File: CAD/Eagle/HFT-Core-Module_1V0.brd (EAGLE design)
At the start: 96.5 x 96.5 mm, 352 parts, among them Q0521 ABS07-32.768KHZ, Q0911 ABM3B-16MHZ-10-R50-1-U, T0801 MMBT2222, T0802 MMBT2222, T0803 MMBT2222, U0111 STM32L4Z_144PIN_SMPS, U0431 PAM2305AAB120, U0601 LM4120IM5-3.0, U0611 MAX5217, U0631 CFPT-141-20MHZ, U0641 OPA354, U0701 Si5338, U0801 NHD-C0220BIZ_2X20CHARS, U0901 AX5243, U1001 AX5243, U1101 MCP3911A0-E-SS, U1111 MAX5136AGTG+, U1121 OPA354, U1131 OPA354, U1141 OPA354, U1601 SOLARPANEL_3V3_5MA1_25MM_X_20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, U1602 SPV1040T, U1701 TS5A23166, U1801 PAM2305AAB330, U1901 TS5A23166, U2001 TS5A23166, U2101 TS5A23166, U2301 MPU-9250, U401 MS5607-02BA03, U501 SHT31-DIS, X0861 TTE_EN11-HSM, X1401 SMA_SMT_AMPHENOL-901-143, X1411 SMA_SMT_AMPHENOL-901-143, X1501 CUI SJ1-3535NS, X1511 CUI SJ1-3535NS, X511 2X20/90_1MM27_HARWIN_M50-3202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, X512 2X20/90_1MM27_HARWIN_M50-3202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, X521 2X20/90_1MM27_HARWIN_M50-3202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, X522 2X20/90_1MM27_HARWIN_M50-3202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, X531 2X20/90_1MM27_HARWIN_M50-3202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, X532 2X20/90_1MM27_HARWIN_M50-3202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

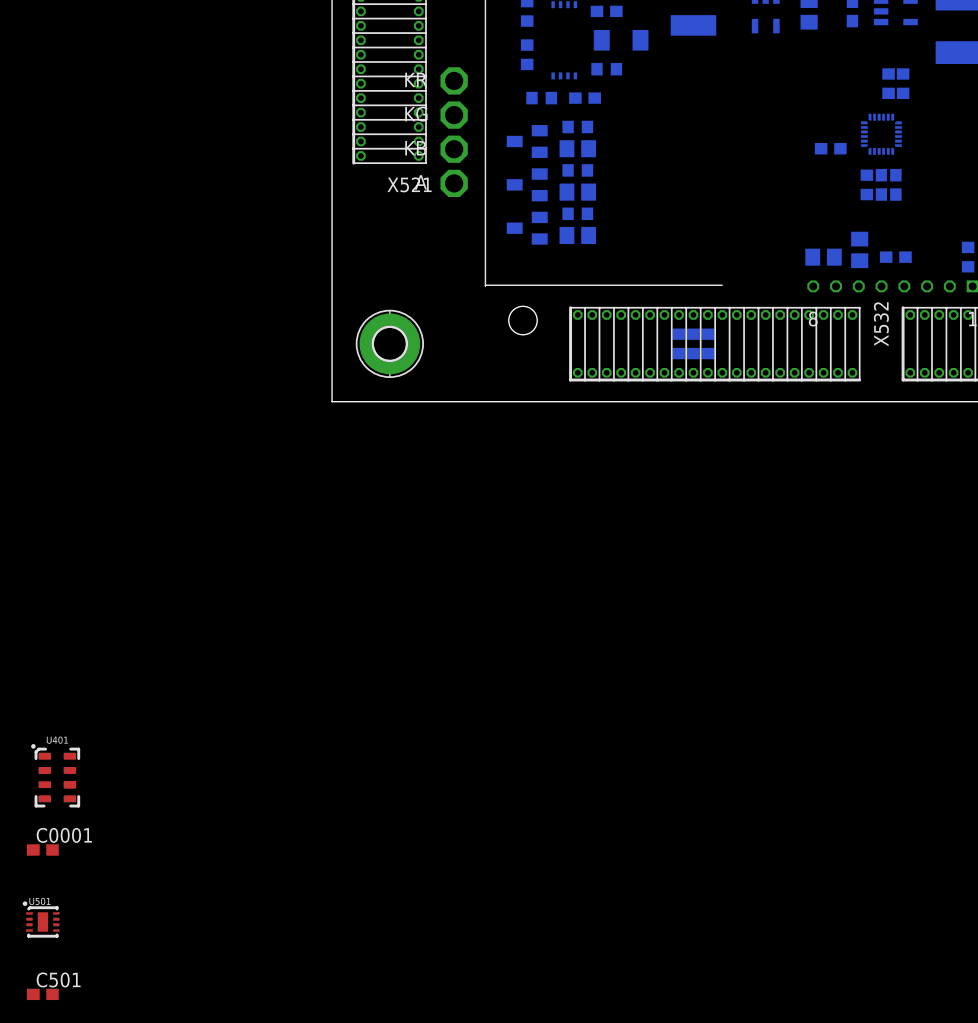
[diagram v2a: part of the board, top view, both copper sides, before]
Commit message: HW_1V0 - SX1276 added to the board - before removing one AX5243
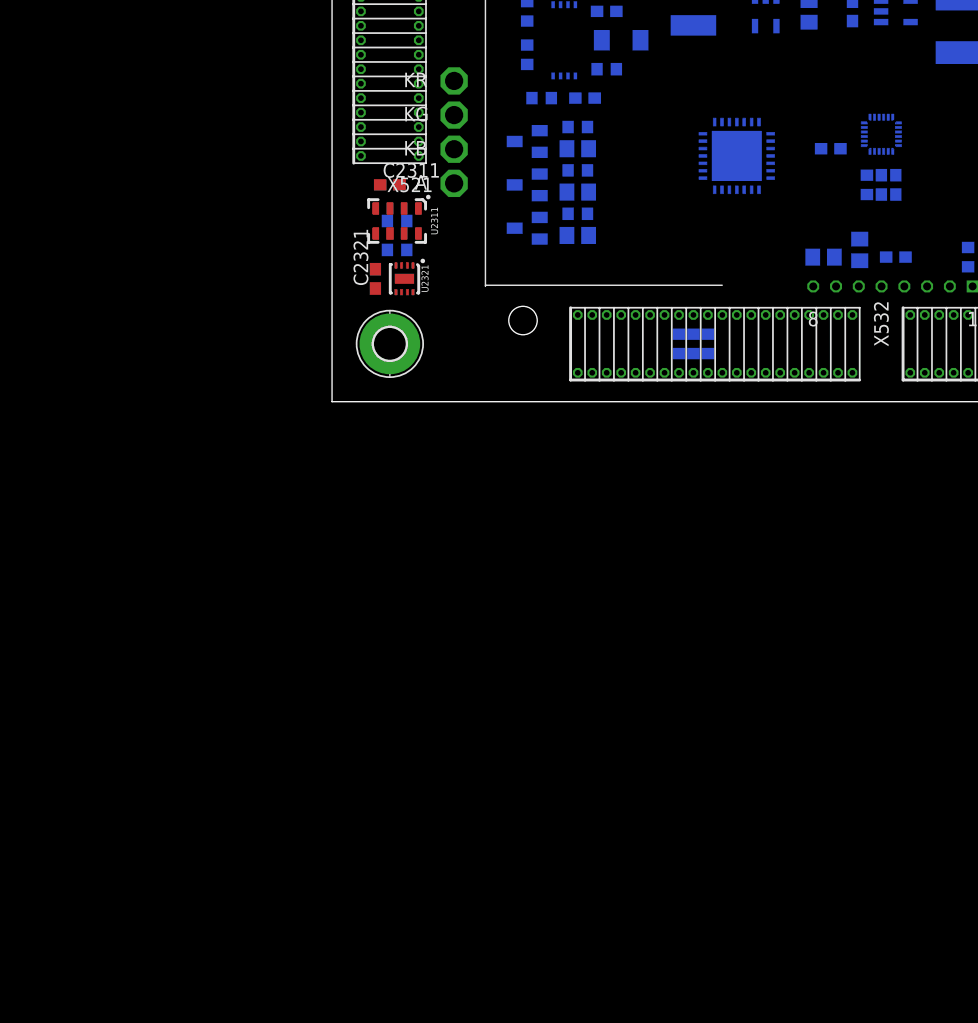
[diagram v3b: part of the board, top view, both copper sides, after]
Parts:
- removed C0001, C501: 100nF, rcl:C0603
- removed R2311, R2312: 3.9kR, rcl:R0603
- removed U401: MS5607-02BA03, df4iah_sensors:MS5607-02BA
- removed U501: SHT31-DIS, df4iah_sensors:DFN8/SHT
- added C2311, C2321: 100nF, rcl:C0603
- added R2331, R2332: 3.9kR, rcl:R0603
- added U2311: MS5607-02BA03, df4iah_sensors:MS5607-02BA
- added U2321: SHT31-DIS, df4iah_sensors:DFN8/SHT
- added U2401: SX1276, df4iah_rf:QFN28-6X6-0P65-PAD
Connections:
- net +3V3: now also C2311.1, C2321.1, R2331.2, R2332.2, U2311.1, U2311.2, U2311.4, U2321.5, U2321.6; no longer C0001.1, C501.1, R2311.2, R2312.2, U401.1, U401.2, U401.4, U501.5, U501.6
- net GND: now also C2311.2, C2321.2, U2311.3, U2321.2, U2321.7, U2321.8, U2321.9, U2401.15, U2401.23, U2401.26, U2401.29; no longer C0001.2, C501.2, U401.3, U501.2, U501.7, U501.8, U501.9
- net MCU_I2C4_SCL: now also R2332.1, U2311.8, U2321.4; no longer R2312.1, U401.8, U501.4
- net MCU_I2C4_SDA: now also R2331.1, U2311.7, U2321.1; no longer R2311.1, U401.7, U501.1

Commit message: HW_1V0_trySX - work-of-the-day for SX1276
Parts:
- removed C1001, C1002, C1003: 100nF, rcl:C0603
- removed C1011: 10pF, rcl:C0603
- removed C1012: 6.8pF, rcl:C0603
- removed C_AX2_A2, C_AX2_A3, C_AX2_B2, C_AX2_F2, C_AX2_M1: 4.7pF, rcl:C0603
- removed C_AX2_C1, C_AX2_C2, C_AX2_M2: 0pF, rcl:C0603
- removed C_AX2_T1, C_AX2_T2: 4.3pF, rcl:C0603
- removed L_AX2_1, L_AX2_B1, L_AX2_B2, L_AX2_F1: 22nH, rcl:R0603
- removed L_AX2_C1, L_AX2_C2: 100nH, rcl:R0603
- removed L_AX2_T1, L_AX2_T2: 43nH, rcl:R0603
- removed R1031, R1032: 100kR, rcl:R0603
- removed R1041, R1051, R1061: 47R, rcl:R0603
- removed TP_AX2_ADC1, TP_AX2_ADC2, TP_AX2_IRQ, TP_AX2_TCXO_EN: PTR1TP06R, testpad:TP06R
- removed U1001: AX5243, df4iah_rf:QFN20-4X4-0P5-PAD
- added C2401: 1u, rcl:C0603
- added C2402, C2403, C2404, C2405, C2406, C2407: 100n, rcl:C0603
- added C2411, C2412: 4.7p, rcl:C0603
- added Q2411: ABM03B-32.000MHZ, df4iah_crystal:ABM03B
- added R2411: 0R, rcl:R0603
- added R2421: 100R, rcl:R0603
- added R2431: 47R, rcl:R0603
- moved U2401 29.3 mm to (64.8, 19.1)
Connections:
- removed net AX2_ADC1: R1031.1, TP_AX2_ADC1.TP, U1001.17
- removed net AX2_ADC2: R1032.1, TP_AX2_ADC2.TP, U1001.18
- removed net AX2_ANTN: C_AX2_C2.1, C_AX2_T2.1, L_AX2_C2.1, U1001.4
- removed net AX2_ANTP: C_AX2_C1.1, C_AX2_T1.1, L_AX2_C1.1, U1001.3
- removed net AX2_B1: C_AX2_M1.1, L_AX2_B1.1, L_AX2_T1.2
- removed net AX2_B2: C_AX2_B2.1, C_AX2_M2.1, L_AX2_B2.2, L_AX2_T2.2
- removed net AX2_CLK16P: C1011.2, C1012.1, U1001.20
- removed net AX2_COMB1: C_AX2_A2.1, C_AX2_B2.2, C_AX2_F2.1, L_AX2_B1.2, L_AX2_F1.1
- removed net AX2_L1: L_AX2_1.1, U1001.8
- removed net AX2_L2: L_AX2_1.2, U1001.7
- removed net AX2_T1: C_AX2_T1.2, L_AX2_T1.1
- removed net AX2_T2: C_AX2_T2.2, L_AX2_T2.1
- removed net AX2_VDD1: C1002.2, U1001.1
- removed net AX2_VDD5: C1003.2, U1001.5
- removed net MCU_AX2_GPO1: R1061.2, TP_AX2_TCXO_EN.TP, U1001.15
- removed net MCU_AX2_IRQ: R1051.2, TP_AX2_IRQ.TP, U1001.14
- removed net MCU_AX2_MISO: R1041.2, U1001.12
- removed net MCU_SPI3_AX2_SEL: R0254.2, U1001.10
- new net MCU_SPI3_SX_SEL: R0254.2, U2401.19
- new net SX_!RESET: R2421.1
- new net SX_!RESET_R: R2421.2, U2401.7
- new net SX_MISO: R2431.2, U2401.17
- new net SX_VR_ANA: C2406.2, U2401.2
- new net SX_VR_DIG: C2407.2, U2401.4
- new net SX_VR_PA: C2405.2, U2401.25
- new net SX_XTA: C2411.1, Q2411.1, U2401.5
- new net SX_XTB: R2411.1, U2401.6
- new net XTB_R: C2412.2, Q2411.3, R2411.2
- net +3V3: now also C2401.1, C2402.2, C2403.2, C2404.2, U2401.14, U2401.24, U2401.3; no longer C1001.1, U1001.16
- net AX1_SYSCLK_R: no longer C1011.1
- net AX2_ANT: no longer C_AX2_A3.1, C_AX2_F2.2, L_AX2_F1.2
- net GND: now also C2401.2, C2402.1, C2403.1, C2404.1, C2405.1, C2406.1, C2407.1, C2411.2, C2412.1, Q2411.2, Q2411.4; no longer C1001.2, C1002.1, C1003.1, C1012.2, C_AX2_A2.2, C_AX2_A3.2, C_AX2_C1.2, C_AX2_C2.2, C_AX2_M1.2, C_AX2_M2.2, L_AX2_B2.1, L_AX2_C1.2, L_AX2_C2.2, R1031.2, R1032.2, U1001.2, U1001.21
- net MCU_SPI3_MOSI: now also U2401.18; no longer U1001.13
- net MCU_SPI3_SCK: now also U2401.16; no longer U1001.11
- net PC11: now also R2431.1; no longer R1041.1
- net PF13: no longer R1061.1
- net PG0: no longer R1051.1

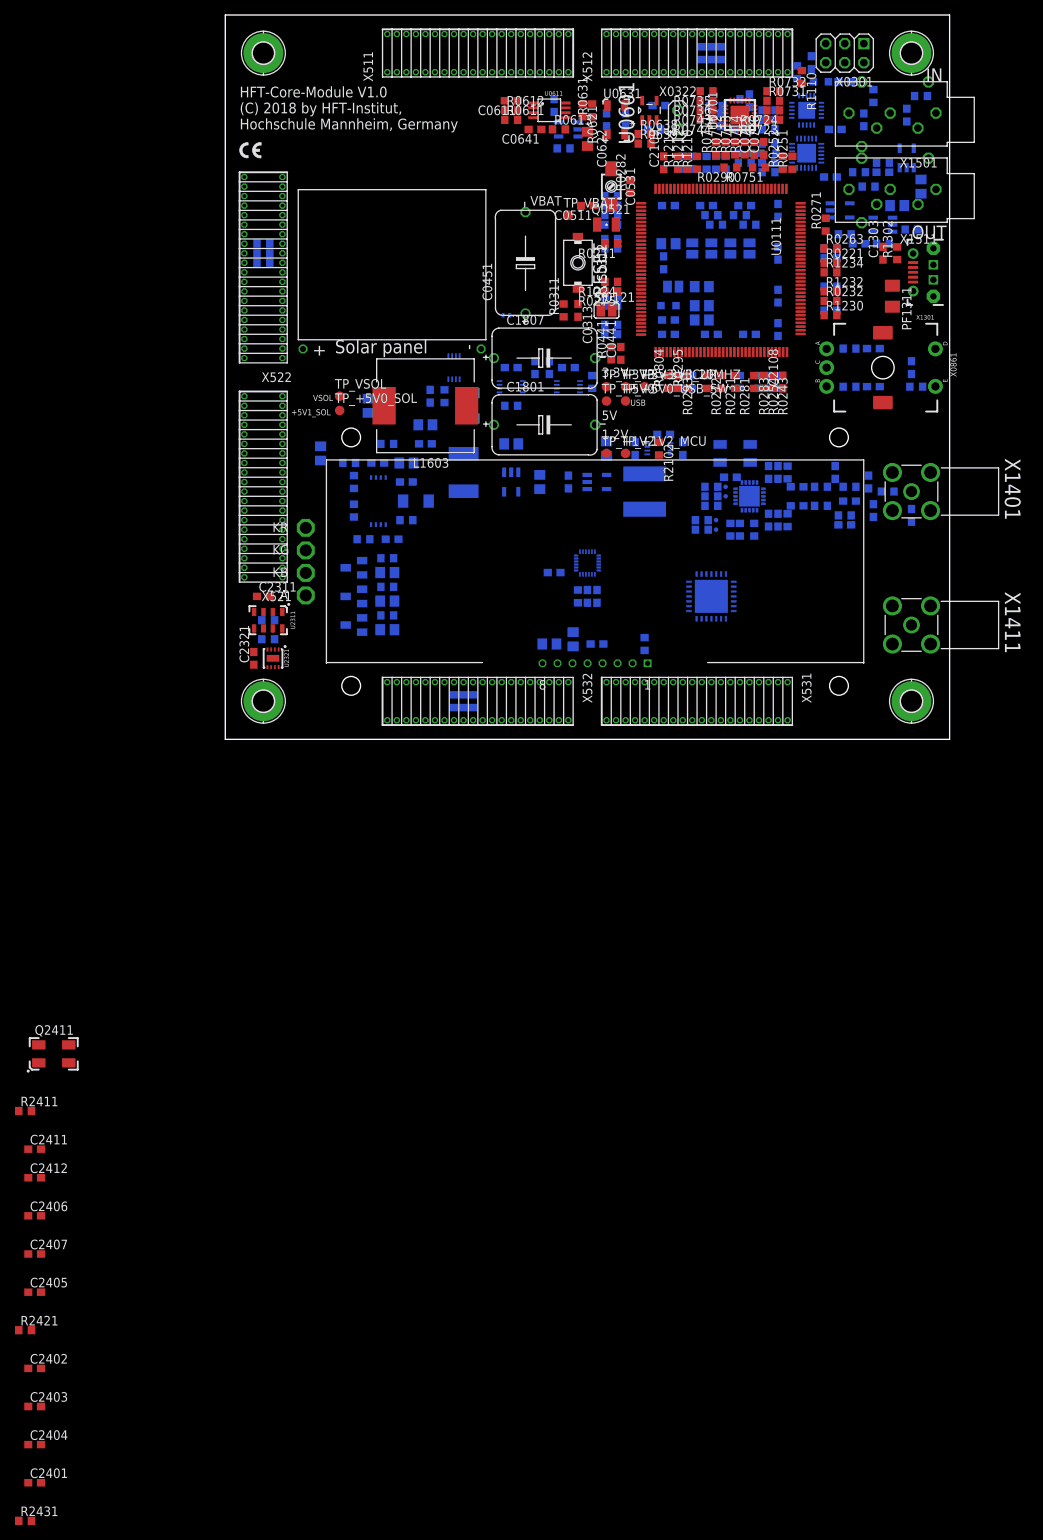
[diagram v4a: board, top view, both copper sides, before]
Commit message: HW_1V0_trySX - reordering and renumbering all parts
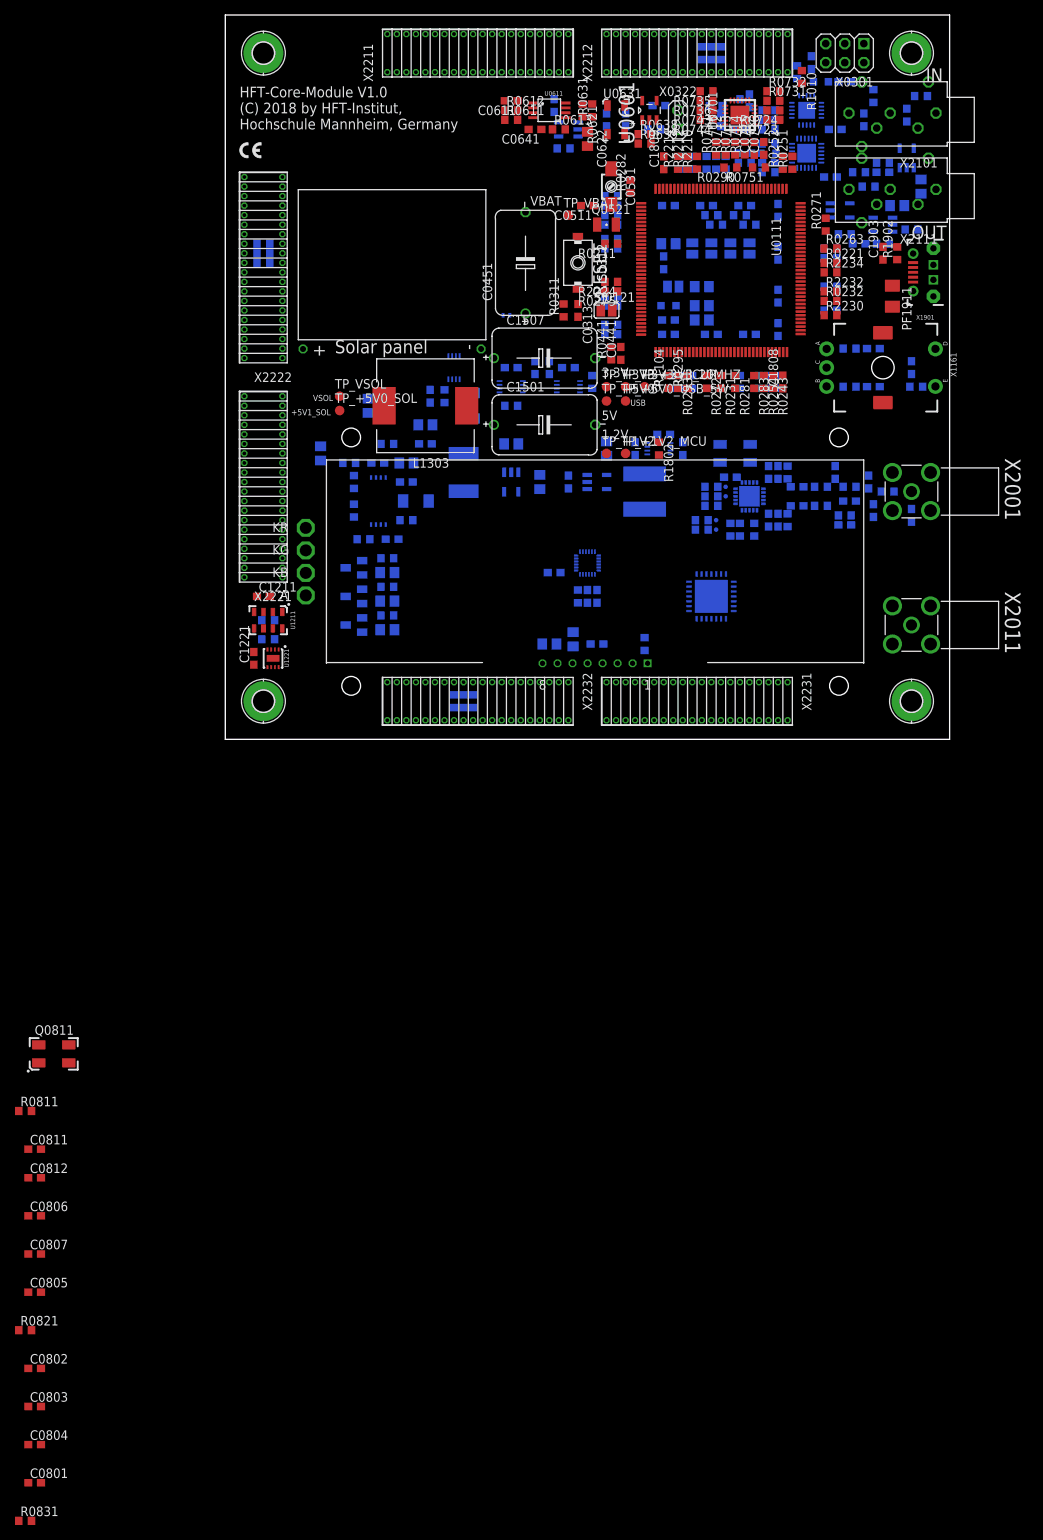
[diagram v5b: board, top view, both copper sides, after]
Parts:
- removed C0831, C1901, C2001, C2003, C2101, C2102: 100nF, rcl:C0603
- removed C2411: 4.7p, rcl:C0603
- removed R0804, R0807: 2.2kR, rcl:R0603
- removed R0805, R0808: 1.8kR, rcl:R0603
- removed R0806, R0809: 10R, rcl:R0805
- removed R0841: 33kR, rcl:R0603
- removed R1302: 330kR, rcl:R0603
- removed R2331, R2332: 3.9kR, rcl:R0603
- removed U1901, U2001, U2101: TS5A23166, df4iah_sc-switches:R-PDSO-G8
- removed U2401: SX1276, df4iah_rf:QFN28-6X6-0P65-PAD
- added C1011, C1401, C1703: 100nF, rcl:C0603
- added C1031: 220nF, df4iah_rcl:C0603
- added C1301: 10uF, rcl:C0805
- added C1501: 1F_EEC-S5R5H105N, df4iah_rcl:W14MM_D8MM_P13MM5
- added C1502: 47uF, rcl:C0805
- added R1004, R1005: 22kR, rcl:R0603
- added R1006, R1007, R1008, R1009, R2231, R2232: 47R, rcl:R0603
- added R1041: 10kR, rcl:R0603
- added R1402: 33kR, rcl:R0603
- added U1001: MCP3911A0-E-SS, df4iah_adc:QFN20_P0MM5_CTRPAD
- added U1301: SOLARPANEL_3V3_5MA1_25MM_X_20MM, df4iah_supply:SOLARPANEL_3V3_5MA1_25MM_X_20MM
- added U1401: TS5A23166, df4iah_sc-switches:R-PDSO-G8
- added U1501: PAM2305AAB330, df4iah_powersupply:SOT95P280X145-5N
- C0811: value 1uF -> 4.7p; device rcl:C0805 -> rcl:C0603
- C1111: value 100nF -> 1uF; device rcl:C0603 -> rcl:C0805
- C1131: value 220nF -> 100nF; device df4iah_rcl:C0603 -> rcl:C0603
- C1303: value 1nF -> 100nF; device df4iah_rcl:C0603 -> rcl:C0603
- C1601: value 10uF -> 100nF; device rcl:C0805 -> rcl:C0603
- C1801: value 1F_EEC-S5R5H105N -> 100nF; device df4iah_rcl:W14MM_D8MM_P13MM5 -> rcl:C0603
- C1802: value 47uF -> 100nF; device rcl:C0805 -> rcl:C0603
- C1903: value 100nF -> 1nF; device rcl:C0603 -> df4iah_rcl:C0603
- R1104: value 22kR -> 2.2kR
- R1105: value 22kR -> 1.8kR
- R1106, R1109: value 47R -> 10R; device rcl:R0603 -> rcl:R0805
- R1107: value 47R -> 2.2kR
- R1108: value 47R -> 1.8kR
- R1141: value 10kR -> 33kR
- R1231, R1232: value 47R -> 3.9kR
- R1902: value 33kR -> 330kR
- U0801: value NHD-C0220BIZ_2X20CHARS -> SX1276; device df4iah_lcd:NHD-C0220BIZ_2X20CHARS -> df4iah_rf:QFN28-6X6-0P65-PAD
- U1101: value MCP3911A0-E-SS -> NHD-C0220BIZ_2X20CHARS; device df4iah_adc:QFN20_P0MM5_CTRPAD -> df4iah_lcd:NHD-C0220BIZ_2X20CHARS
- U1601: value SOLARPANEL_3V3_5MA1_25MM_X_20MM -> TS5A23166; device df4iah_supply:SOLARPANEL_3V3_5MA1_25MM_X_20MM -> df4iah_sc-switches:R-PDSO-G8
- U1801: value PAM2305AAB330 -> TS5A23166; device df4iah_powersupply:SOT95P280X145-5N -> df4iah_sc-switches:R-PDSO-G8
- moved C0811 96.1 mm to (-25.4, -54.6), flipped to the top, turned to 0 degrees
- moved R1105 92.0 mm to (21.6, 20.3), turned to 0 degrees
- moved R1232 88.1 mm to (5.71, 13.3), flipped to the bottom
- moved R1231 85.5 mm to (5.71, 15.9), turned to 0 degrees
- moved R1109 83.8 mm to (21.6, 14.6)
- moved R1108 83.3 mm to (21.6, 16.5)
- moved R1106 82.8 mm to (21.6, 18.4)
- moved C1131 73.5 mm to (49.5, 12.7)
- moved C1303 70.4 mm to (24.1, 34.3), flipped to the bottom, turned to 180 degrees
- moved C1111 70.4 mm to (43.2, 12.7), turned to 180 degrees
- moved U1101 66.0 mm to (49.3, 24.1), flipped to the top
- moved R1141 60.8 mm to (55.9, 12.7), turned to 270 degrees
- moved R1104 50.8 mm to (59.1, 47.6), flipped to the top, turned to 90 degrees
- moved C1903 47.0 mm to (87.6, 64.8), flipped to the top
- moved R1902 44.1 mm to (89.5, 64.8), flipped to the top, turned to 90 degrees
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- renumbered C0821 to C1121, C0861 to C1161, C0862 to C1162, C0871 to C1171, C1101 to C1001, C1102 to C1002, C1103 to C1003, C1104 to C1004, C1105 to C1005, C1112 to C1012, C1113 to C1013, C1132 to C1032, C1141 to C1041, C1142 to C1042, C1602 to C1302, C1604 to C1304, C1605 to C1305, C1606 to C1306, C1805 to C1505, C1806 to C1506, C1807 to C1507, C2103 to C1803, C2108 to C1808, C2109 to C1809, C2301 to C1201, C2302 to C1202, C2303 to C1203, C2311 to C1211, C2321 to C1221, C2401 to C0801, C2402 to C0802, C2403 to C0803, C2404 to C0804, C2405 to C0805, C2406 to C0806, C2407 to C0807, C2412 to C0812, D1603 to D1303, D1701 to D1401, H2201 to H2301, H2202 to H2302, H2203 to H2303, H2204 to H2304, L1102 to L1002, L1112 to L1012, L1603 to L1303, L1804 to L1504, PF1311 to PF1911, Q2411 to Q0811, R0801 to R1101, R0802 to R1102, R0803 to R1103, R0861 to R1161, R0862 to R1162, R0871 to R1171, R1110 to R1010, R1114 to R1014, R1131 to R1031, R1132 to R1032, R1135 to R1035, R1142 to R1042, R1145 to R1045, R1210 to R2210, R1211 to R2211, R1212 to R2212, R1213 to R2213, R1214 to R2214, R1215 to R2215, R1216 to R2216, R1217 to R2217, R1220 to R2220, R1221 to R2221, R1222 to R2222, R1223 to R2223, R1224 to R2224, R1225 to R2225, R1226 to R2226, R1227 to R2227, R1230 to R2230, R1233 to R2233, R1234 to R2234, R1235 to R2235, R1236 to R2236, R1237 to R2237, R1604 to R1304, R1605 to R1305, R1606 to R1306, R1607 to R1307, R1608 to R1308, R1609 to R1309, R2002 to R1602, R2102 to R1802, R2301 to R1201, R2411 to R0811, R2421 to R0821, R2431 to R0831, T0801 to T1101, T0802 to T1102, T0803 to T1103, U1111 to U1011, U1121 to U1021, U1131 to U1031, U1141 to U1041, U1602 to U1302, U2301 to U1201, U2311 to U1211, U2321 to U1221, X0861 to X1161, X1301 to X1901, X1401 to X2001, X1411 to X2011, X1501 to X2101, X1511 to X2111, X511 to X2211, X512 to X2212, X521 to X2221, X522 to X2222, X531 to X2231, X532 to X2232
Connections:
- net +1V2: now also C1801.1, U1801.1, U1801.5; no longer C2101.1, U2101.1, U2101.5
- net +3V3: now also C1131.1, C1601.1, C1701.1, C1802.1, R1231.2, R1232.2, U0801.14, U0801.24, U0801.3, U1101.12, U1101.5, U1501.4, U1601.1, U1601.5, U1601.8, U1701.1, U1701.5, U1701.8, U1801.8; no longer C0831.1, C1901.1, C2001.1, C2102.1, R2331.2, R2332.2, U0801.12, U0801.5, U1801.4, U1901.1, U1901.5, U1901.8, U2001.1, U2001.5, U2001.8, U2101.8, U2401.14, U2401.24, U2401.3
- net +3V3_20MHZ: now also C1703.1, U1701.2, U1701.6; no longer C1903.1, U1901.2, U1901.6
- net +3V3_HICUR: now also C1011.1, C1603.1, U1001.19, U1601.2, U1601.6; no longer C1111.1, C2003.1, U1101.19, U2001.2, U2001.6
- net +5V0: now also C1501.+, C1502.1, U1501.1, U1501.3; no longer C1801.+, C1802.1, U1801.1, U1801.3
- net GND: now also C0811.2, C1011.2, C1131.2, C1301.2, C1303.2, C1401.2, C1501.-, C1502.2, C1703.2, C1801.2, C1903.1, R1004.1, R1005.1, R1106.1, R1108.1, R1109.1, R1141.1, R1402.1, U0801.15, U0801.23, U0801.26, U0801.29, U1001.2, U1001.21, U1001.4, U1001.5, U1001.7, U1001.8, U1301.-VSOL, U1401.4, U1501.2, U1601.4, U1801.4; no longer C0831.2, C1111.2, C1303.1, C1801.-, C1901.2, C1903.2, C2001.2, C2003.2, C2101.2, C2102.2, C2411.2, R0805.1, R0806.1, R0808.1, R0809.1, R0841.1, R1104.1, R1302.1, U0801.4, U1101.2, U1101.21, U1101.5, U1101.7, U1101.8, U1601.-VSOL, U1801.2, U1901.4, U2001.4, U2101.4, U2401.15, U2401.23, U2401.26, U2401.29
- net LCD_C1+: now also C1111.2, U1101.7; no longer C0811.2, U0801.7
- net LCD_C1-: now also C1111.1, U1101.8; no longer C0811.1, U0801.8
- net LCD_VOUT: now also U1101.6; no longer U0801.6
- net LED_B_B: now also R1107.1, R1108.2; no longer R0807.1, R0808.2
- net LED_B_E: now also R1109.2; no longer R0809.2
- net LED_B_K: now also U1101.11; no longer U0801.11
- net LED_G_B: now also R1104.1, R1105.2; no longer R0804.1, R0805.2
- net LED_G_E: now also R1106.2; no longer R0806.2
- net LED_G_K: now also U1101.10; no longer U0801.10
- net LED_R_K: now also U1101.9; no longer U0801.9
- net MAX5136_OUT0_R: now also C1031.1; no longer C1131.1
- net MAX5136_OUT0_SUM: now also C1031.2; no longer C1131.2
- net MAX5136_OUT1: now also R1041.1; no longer R1141.1
- net MAX5136_OUT1_R: now also R1041.2; no longer R1141.2
- net MCP3911_!DR: now also R1006.1, U1001.11; no longer R1106.1, U1101.11
- net MCP3911_CH0+: now also R1004.2, U1001.1; no longer R1104.2, U1101.1
- net MCP3911_CH1+: now also R1005.2, U1001.3; no longer R1105.2, U1101.3
- net MCP3911_MDAT0: now also R1008.1, U1001.10; no longer R1108.1, U1101.10
- net MCP3911_MDAT1: now also R1009.1, U1001.9; no longer R1109.1, U1101.9
- net MCP3911_REFINOUT: now also U1001.6; no longer U1101.6
- net MCP3911_SDO: now also R1007.1, U1001.16; no longer R1107.1, U1101.16
- net MCU_20MHZ_EN: now also R1702.2, U1701.3, U1701.7; no longer R1902.2, U1901.3, U1901.7
- net MCU_HICUR_EN: now also U1601.3, U1601.7; no longer U2001.3, U2001.7
- net MCU_I2C4_SCL: now also R1232.1, U1101.2; no longer R2332.1, U0801.2
- net MCU_I2C4_SDA: now also R1231.1, U1101.3; no longer R2331.1, U0801.3
- net MCU_LCD_!RST: now also R1141.2, U1101.1; no longer R0841.2, U0801.1
- net MCU_SPI3_AUDIO_ADC_!RESET: now also U1001.18; no longer U1101.18
- net MCU_SPI3_AUDIO_ADC_SEL: now also U1001.14; no longer U1101.14
- net MCU_SPI3_MOSI: now also U0801.18, U1001.17; no longer U1101.17, U2401.18
- net MCU_SPI3_SCK: now also U0801.16, U1001.15; no longer U1101.15, U2401.16
- net MCU_SPI3_SX_SEL: now also U0801.19; no longer U2401.19
- net MCU_VDD12: now also U1801.2, U1801.6; no longer U2101.2, U2101.6
- net MCU_VDD12_EN: now also U1801.3, U1801.7; no longer U2101.3, U2101.7
- net MCU_VUSB_EN: now also R1402.2, U1401.3, U1401.7; no longer R1702.2, U1701.3, U1701.7
- net MVP3911_AVDD: now also U1001.20; no longer U1101.20
- net PA7: now also R1104.2; no longer R0804.2
- net PB0: now also R1107.2; no longer R0807.2
- net PC11: now also R1007.2; no longer R1107.2
- net PD0: now also R1009.2; no longer R1109.2
- net PD1: now also R1008.2; no longer R1108.2
- net PD10: now also R2231.1; no longer R1231.1
- net PD14: now also R2232.1; no longer R1232.1
- net PD2: now also R1006.2; no longer R1106.2
- net PH0_OSC_IN: now also U1001.12; no longer U1101.12
- net PS01: now also R2231.2; no longer R1231.2
- net PS02: now also R2232.2; no longer R1232.2
- net SPV_VOUT: now also C1303.1; no longer C1603.1
- net SW: now also U1501.5; no longer U1801.5
- net SX_!RESET_R: now also U0801.7; no longer U2401.7
- net SX_MISO: now also U0801.17; no longer U2401.17
- net SX_VR_ANA: now also U0801.2; no longer U2401.2
- net SX_VR_DIG: now also U0801.4; no longer U2401.4
- net SX_VR_PA: now also U0801.25; no longer U2401.25
- net SX_XTA: now also C0811.1, U0801.5; no longer C2411.1, U2401.5
- net SX_XTB: now also U0801.6; no longer U2401.6
- net USB_SHIELD: now also C1903.2, R1902.2; no longer C1303.2, R1302.2
- net VDDUSB: now also C1401.1, U1401.1, U1401.5, U1401.8; no longer C1701.1, U1701.1, U1701.5, U1701.8
- net VSOL: now also C1301.1, U1301.+VSOL; no longer C1601.1, U1601.+VSOL
- net VUSB_SW: now also U1401.2, U1401.6; no longer U1701.2, U1701.6
